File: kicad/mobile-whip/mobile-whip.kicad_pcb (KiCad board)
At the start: 2 copper layers, 200 x 22 mm, 50 parts, among them J1 Conn_Coaxial, J2 USB_C_Receptacle_USB2.0, Q1 SI2301CDS-T1-GE3, Q2 SI2301CDS-T1-GE3, SW1 MK-12C02-G025, U1 LTC6268IS6, U2 TP4054, U3 LP2985-3.3, U4 TLV431

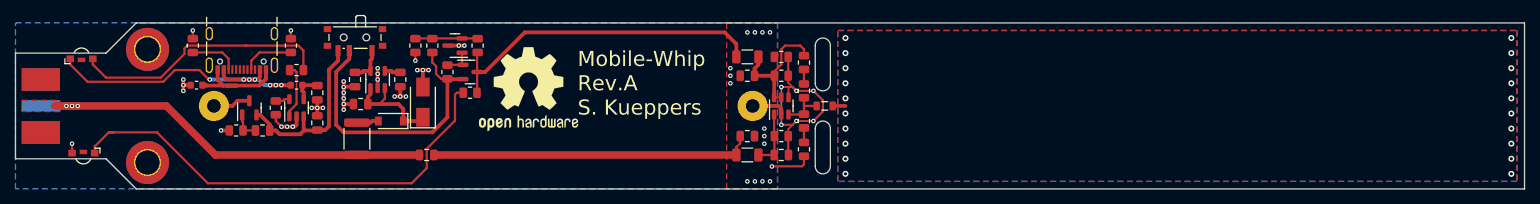
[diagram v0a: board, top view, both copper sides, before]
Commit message: Added LCSC part numbers
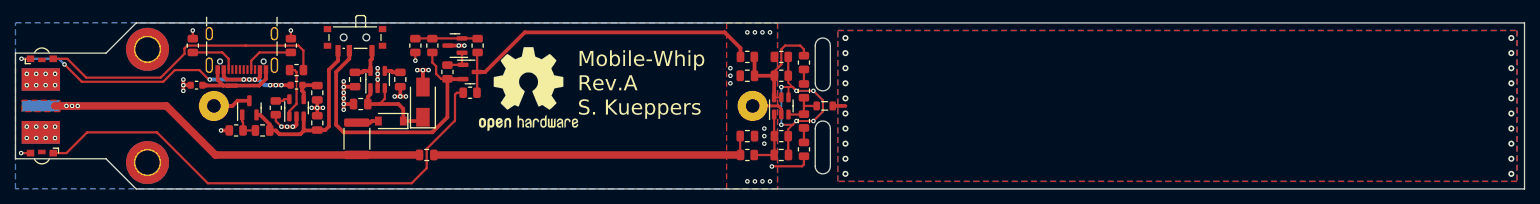
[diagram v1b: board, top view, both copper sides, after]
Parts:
- C2: value 1uF/25V -> 10uF/25V
- C4: value 10pF -> 47pF
- C5: value 100nF -> 10nF
- R1, R2, R3, R4: value 10Meg -> 1Meg
- R15: value 2.2R -> 1R; footprint Resistor_SMD:R_1206_3216Metric -> Resistor_SMD:R_0805_2012Metric
- R16: value 330K -> 220K
- R9: footprint Resistor_SMD:R_1206_3216Metric -> Resistor_SMD:R_0805_2012Metric
- moved D1 5.50 mm to (53.5, 86.2)
- moved D2 5.25 mm to (53.5, 73.8)
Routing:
- net VBUS: track 42.2 -> 49.3 mm, vias 7 -> 9
- net Net-(D2-Pad1): track 34.7 -> 39.5 mm
- net Net-(D1-Pad2): track 62.3 -> 66.8 mm
- net GND: vias 46 -> 62
